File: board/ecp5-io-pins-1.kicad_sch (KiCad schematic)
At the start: 9 parts

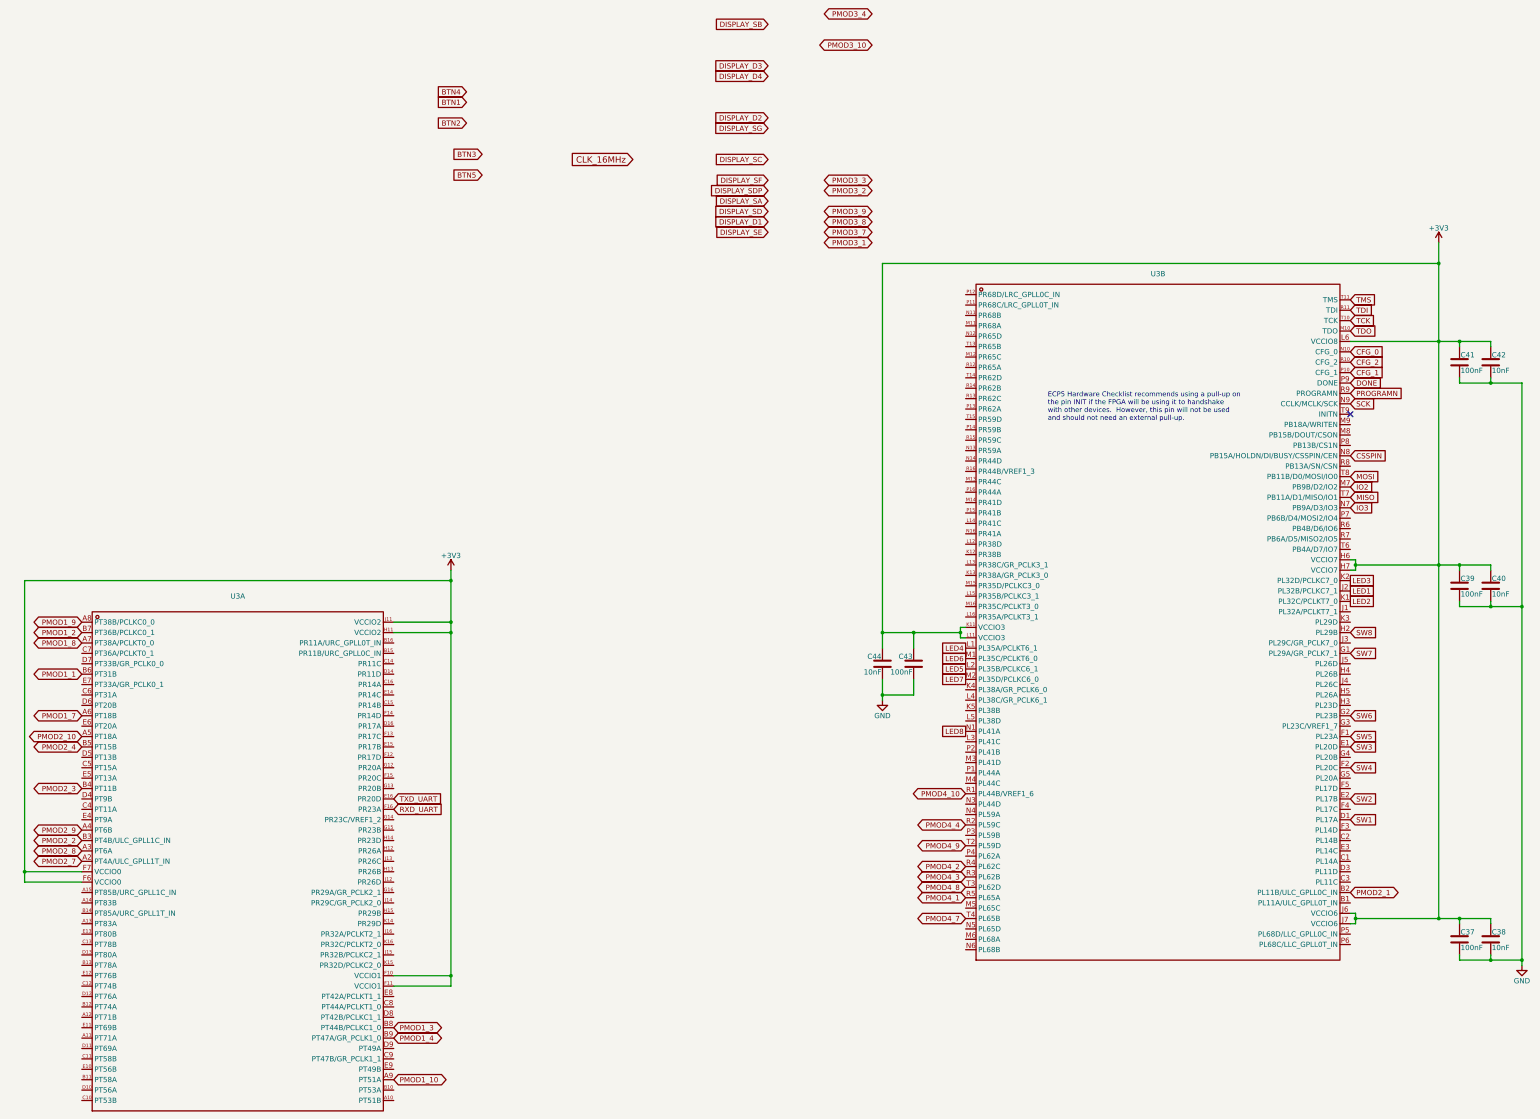
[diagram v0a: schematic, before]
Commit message: Change LFE5U chip from BGA381 to BGA256 package
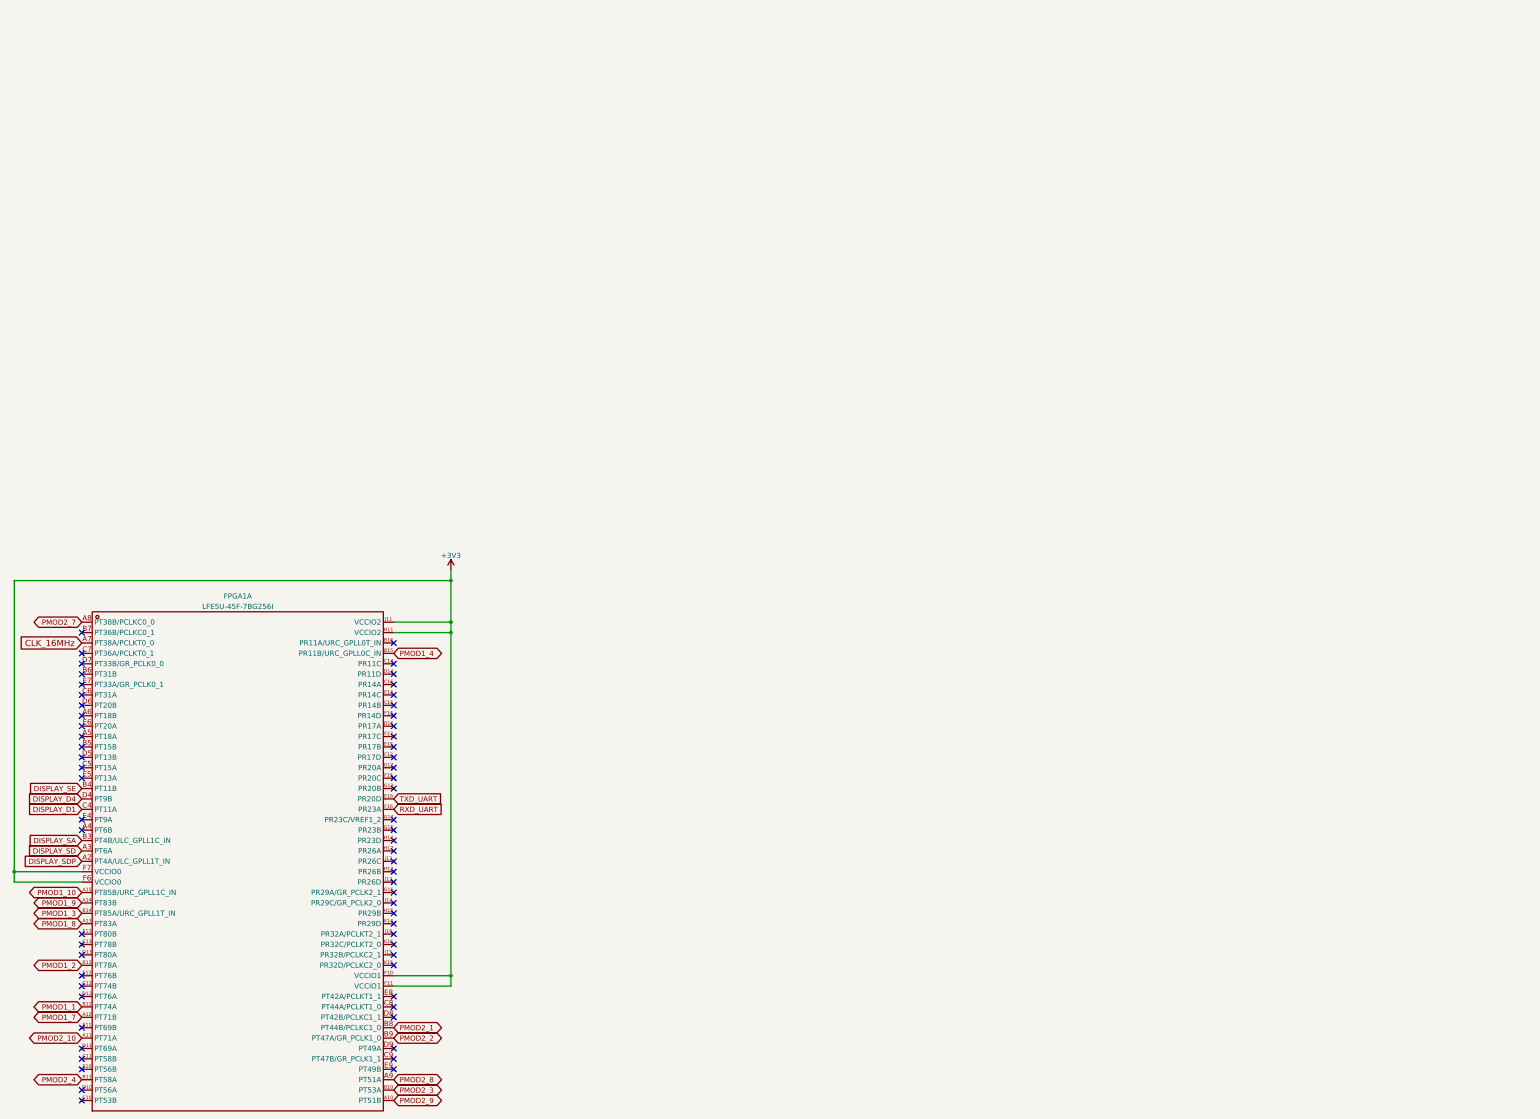
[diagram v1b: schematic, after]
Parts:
- removed C37, C39, C41, C43: 100nF, Capacitor_SMD:C_0402_1005Metric, symbol Device:C
- removed C38, C40, C42, C44: 10nF, Capacitor_SMD:C_0402_1005Metric, symbol Device:C
- removed unit 2 of U3
- FPGA1: renamed from U3; value ~ -> LFE5U-45F-7BG256I; JLC (none) -> CABGA-256; LCSC (none) -> C1550826
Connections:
- net CLK_16MHz: now also FPGA1.A7 (PT38A/PCLKT0_0)
- net DISPLAY_D1: now also FPGA1.C4 (PT11A)
- net DISPLAY_D4: now also FPGA1.D4 (PT9B)
- net DISPLAY_SA: now also FPGA1.B3 (PT4B/ULC_GPLL1C_IN)
- net DISPLAY_SD: now also FPGA1.A3 (PT6A)
- net DISPLAY_SDP: now also FPGA1.A2 (PT4A/ULC_GPLL1T_IN)
- net DISPLAY_SE: now also FPGA1.B4 (PT11B)
- net PMOD1_1: now also FPGA1.B12 (PT74A); no longer FPGA1.B6 (PT31B)
- net PMOD1_10: now also FPGA1.A15 (PT85B/URC_GPLL1C_IN); no longer FPGA1.A9 (PT51A)
- net PMOD1_2: now also FPGA1.B13 (PT78A); no longer FPGA1.B7 (PT36B/PCLKC0_1)
- net PMOD1_3: now also FPGA1.B14 (PT85A/URC_GPLL1T_IN); no longer FPGA1.B8 (PT44B/PCLKC1_0)
- net PMOD1_4: now also FPGA1.B15 (PR11B/URC_GPLL0C_IN); no longer FPGA1.B9 (PT47A/GR_PCLK1_0)
- net PMOD1_7: now also FPGA1.A12 (PT71B); no longer FPGA1.A6 (PT18B)
- net PMOD1_8: now also FPGA1.A13 (PT83A); no longer FPGA1.A7 (PT38A/PCLKT0_0)
- net PMOD1_9: now also FPGA1.A14 (PT83B); no longer FPGA1.A8 (PT38B/PCLKC0_0)
- net PMOD2_1: now also FPGA1.B8 (PT44B/PCLKC1_0)
- net PMOD2_10: now also FPGA1.A11 (PT71A); no longer FPGA1.A5 (PT18A)
- net PMOD2_2: now also FPGA1.B9 (PT47A/GR_PCLK1_0); no longer FPGA1.B3 (PT4B/ULC_GPLL1C_IN)
- net PMOD2_3: now also FPGA1.B10 (PT53A); no longer FPGA1.B4 (PT11B)
- net PMOD2_4: now also FPGA1.B11 (PT58A); no longer FPGA1.B5 (PT15B)
- net PMOD2_7: now also FPGA1.A8 (PT38B/PCLKC0_0); no longer FPGA1.A2 (PT4A/ULC_GPLL1T_IN)
- net PMOD2_8: now also FPGA1.A9 (PT51A); no longer FPGA1.A3 (PT6A)
- net PMOD2_9: now also FPGA1.A10 (PT51B); no longer FPGA1.A4 (PT6B)
- no-connect marks 1 -> 63
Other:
- note removed: "ECP5 Hardware Checklist recommends using a pull-up on the pin INIT if the FPGA will be using it to handshake with other devices. However, this pin will not be used and should not need an external pull-up."
